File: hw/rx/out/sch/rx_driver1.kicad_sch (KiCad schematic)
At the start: 24 parts, among them U6 OPA1656

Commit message: hw/rx: review fixes for #81 (mute relay + supervisor, S1J clamps, VCM discharge + 2-pole filter, 16 V LDOs, keyed header, I2S DNP, cable stability + power-cycle SPICE, FLT low latency) (#32)
Co-Authored-By: Claude Opus 5.5 <noreply@anthropic.com>
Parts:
- added C49: 22u 25V, Capacitor_SMD:CP_Elec_5x5.4, symbol openpack_rx:CP
- added D5, D6: S1J, Diode_SMD:D_SMA, symbol openpack_rx:Diode
- added D8: BAT54, Package_TO_SOT_SMD:SOT-23, symbol openpack_rx:BAT54
- added K1: TQ2SA-12V, openpack:Panasonic_TQ2SA, symbol openpack_rx:Relay_TQ2
- added R53, R54, R55: 10k, Resistor_SMD:R_0402_1005Metric, symbol openpack_rx:R
- C43: value 47u 25V -> 22u 25V; MPN ALU_47u_25V -> ALU_22u_25V
- D3, D4: value BAV99 -> S1J; footprint Package_TO_SOT_SMD:SOT-23 -> Diode_SMD:D_SMA; symbol openpack_rx:BAV99 -> openpack_rx:Diode; MPN BAV99,215 -> S1J
- R45, R46: value 100k -> 22k
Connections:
- net +12VA: now also C41.2, C44.1, R42.2, R43.1, R47.1, U6.1 (OUTA), U6.3 (+INA), U6.5 (+INB), C49.1 (+), D5.1 (K), D6.1 (K), D8.1 (A), D8.3 (K), R53.2; no longer D3.2 (K2), D4.2 (K2)
- net GND: now also C43.1 (+), D3.2 (A), D4.2 (A), R45.2, R46.1, C49.2 (-), R53.1, R54.2, R55.2; no longer C40.2 (-), C42.1, C42.2, C47.1, C48.1, D3.1 (A1), D3.3 (COM), D4.1 (A1), D4.3 (COM), R43.2, R44.1, R44.2, R47.2, R50.1, R50.2, U6.6 (-INB), U6.7 (OUTB)
- net DRV_CIN: now reaches C40.1 (+), R41.1
- net DRV_HOT_O: now reaches R51.1, R52.1
- net DRV_HOT_O: now also K1.7 (NO2); no longer C48.2
- net DRV_COLD_O: now reaches R48.1, R49.1
- net DRV_COLD_O: now also K1.4 (NO1); no longer C47.2
- removed net DRV_OUTA: C41.2, C43.1 (+), C44.1, R42.2, R43.1, R45.2, R46.1, R47.1, U6.1 (OUTA), U6.3 (+INA), U6.5 (+INB)
- new net +12V: K1.1 (COIL+)
- new net DAC_OUTF: C40.2 (-)
- new net DRV_COLD_P: C47.1, D3.1 (K), D5.2 (A), R47.2
- new net DRV_COLD_X: C47.2, K1.3 (COM1), R54.1
- new net DRV_HOT_P: C42.1, C42.2, C48.1, D4.1 (K), D6.2 (A), R43.2, R44.1, R44.2, R50.1, R50.2, U6.6 (-INB), U6.7 (OUTB)
- new net DRV_HOT_X: C48.2, K1.8 (COM2), R55.1
- new net RLY_COIL: K1.10 (COIL-)
- no-connect marks 0 -> 5
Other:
- moved on the sheet: C40, C41, C42, C43, C44, C45, C46, C47, C48, R41, R42, R43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

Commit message: hw/rx: receiver module BT40NE -> BT40E, FEM node pack-only (ADR-0021, #112)
- hw/rx: BT40E symbol (Fanstel v1.09 p.14 pad map = BT40F/NE names), footprint
  openpack:Fanstel_BT40E (14x16 mm), no FEM nets, P1.05 open; GPIO map unchanged.
  ERC 0/0. BOM: Digi-Key UK GBP 9.7765 q100 -> $30.68 / GBP 23.38 per sub-board.
- fw: receiver builds add boards/role_rx_cpunet.overlay (FEM node disabled, no
  &radio fem); rx.c refuses to build with the FEM enabled.
- ADR-0014 amended (datasheet checks, FCC X8WBT40F, no UKCA DoC, BOM).

Co-Authored-By: Claude Opus 5.5 <noreply@anthropic.com>
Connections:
- net DRV_HOT_P is gone; now on net DAC_OUTF: C42.1, C42.2, C48.1, D4.1 (K), D6.2 (A), R43.2, R44.1, R44.2, R50.1, R50.2, U6.6 (-INB), U6.7 (OUTB)
- net +12VA: no longer C41.2, C44.1, C49.1 (+), D8.1 (A), R42.2, R43.1, R47.1, R53.2, U6.1 (OUTA), U6.3 (+INA), U6.5 (+INB)
- net DRV_CIN: no longer names the net of C40.1 (+), R41.1
- new net DRV_OUTA: C41.2, C44.1, C49.1 (+), D8.1 (A), R42.2, R43.1, R47.1, R53.2, U6.1 (OUTA), U6.3 (+INA), U6.5 (+INB)
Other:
- moved on the sheet: C40, C41, C42, C43, C44, C45, C46, C47, C48, C49, D3, D4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

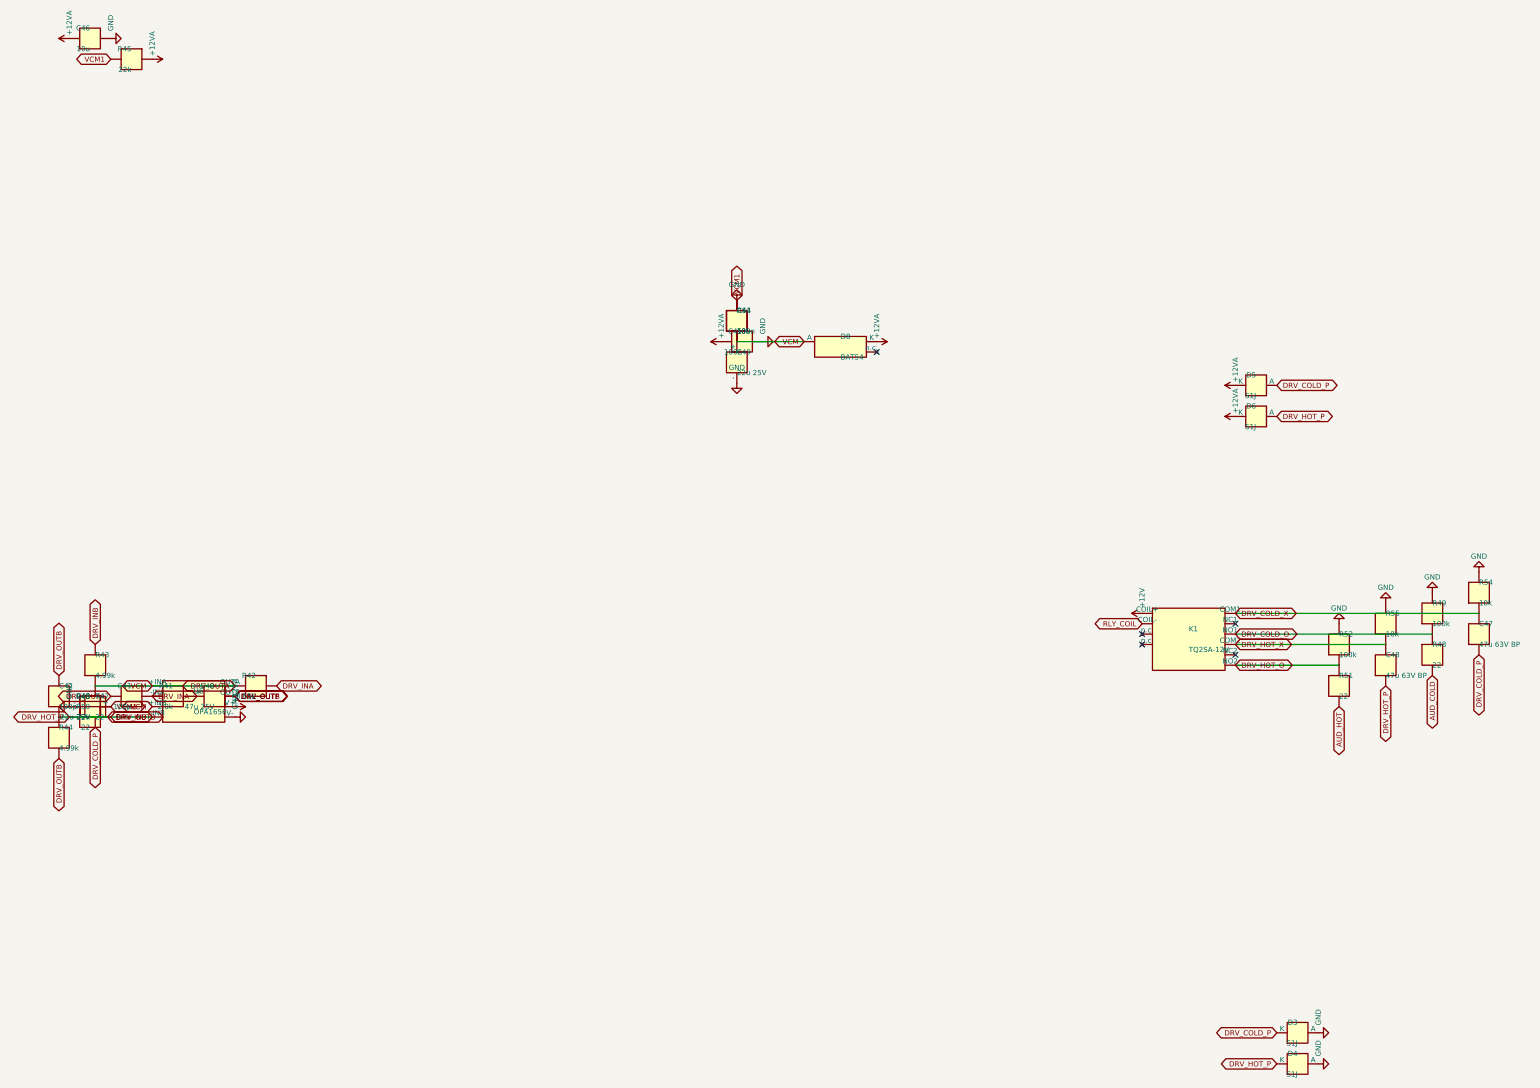
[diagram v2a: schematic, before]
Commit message: hw/rx: receiver sub-board layout, 50 ohm GCPW, keyed J1, JLC rules that load, fab outputs (#34) (#116)
Part of #34. Receiver layout (48x90 mm, DRC 0/0), #116 independent-review fixes (netclass pour clearances in rx + pack, no hole at J1 pin 14, solid RF grounds, K1 pin-1/CPL), every placed part with a checked LCSC code.

Co-Authored-By: Claude Opus 5.5 <noreply@anthropic.com>
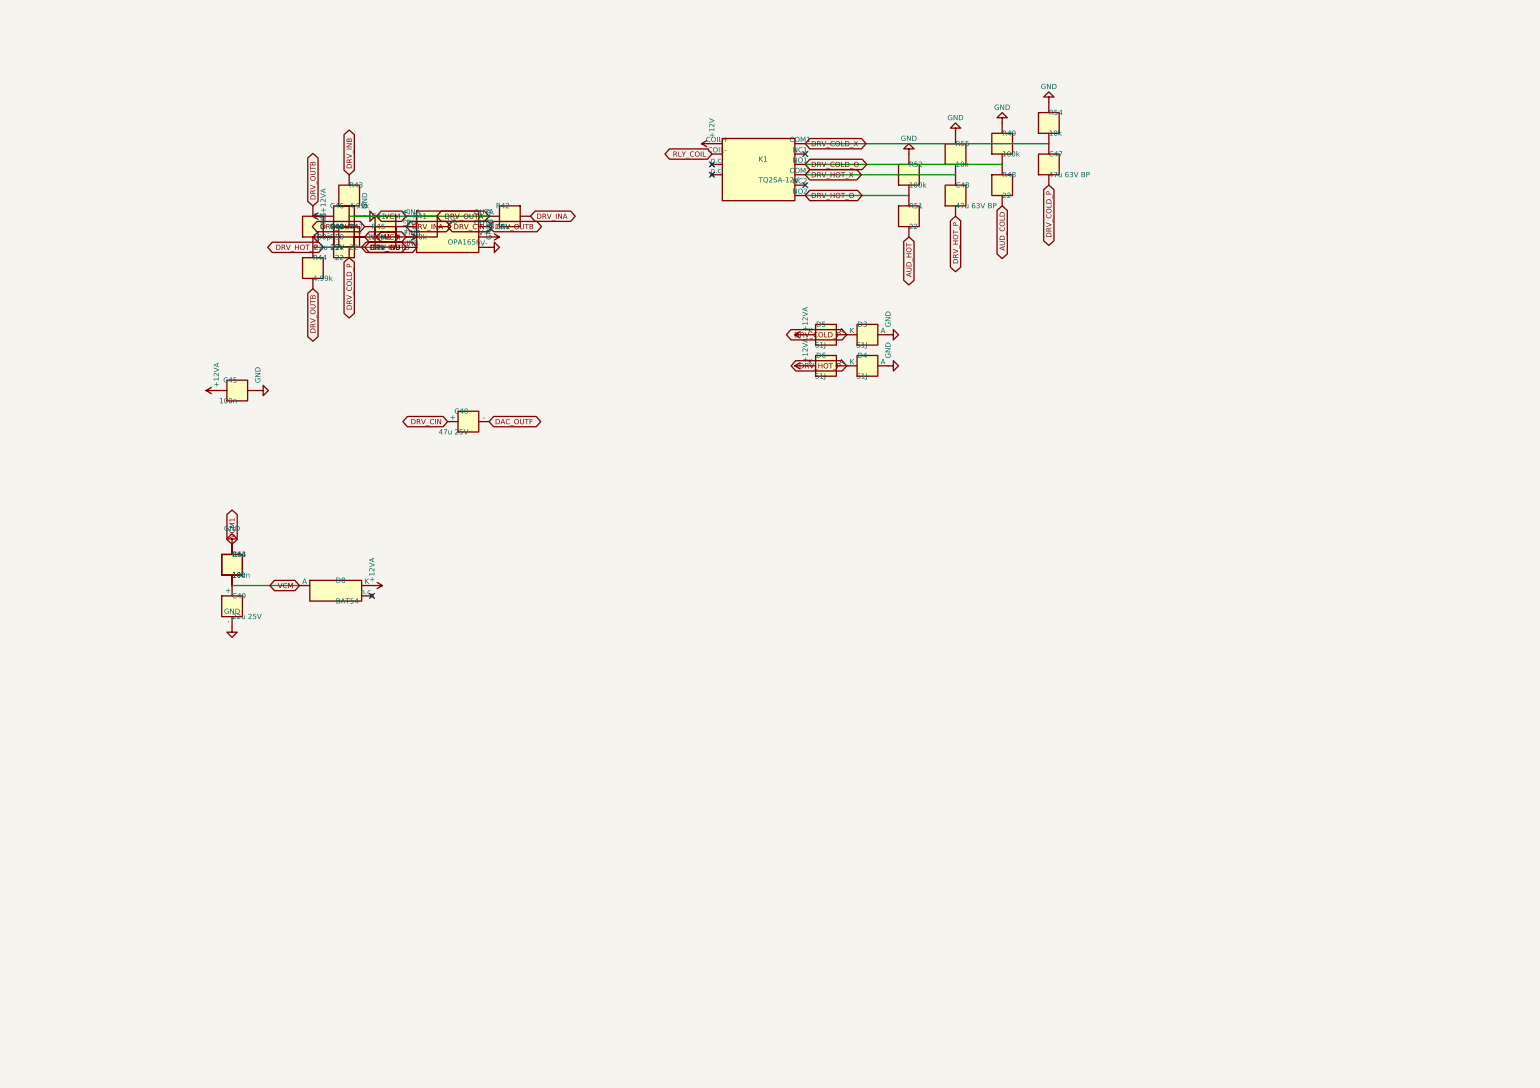
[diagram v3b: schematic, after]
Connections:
- net DRV_OUTA is gone; now on net +12VA: C41.2, C44.1, C49.1 (+), D8.1 (A), R42.2, R43.1, R47.1, R53.2, U6.1 (OUTA), U6.3 (+INA), U6.5 (+INB)
- net DAC_OUTF: no longer C42.1, C42.2, C48.1, D4.1 (K), D6.2 (A), R43.2, R44.1, R44.2, R50.1, R50.2, U6.6 (-INB), U6.7 (OUTB)
- net DRV_CIN: now reaches C40.1 (+), R41.1
- new net DRV_HOT_P: C42.1, C42.2, C48.1, D4.1 (K), D6.2 (A), R43.2, R44.1, R44.2, R50.1, R50.2, U6.6 (-INB), U6.7 (OUTB)
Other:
- moved on the sheet: C40, C41, C42, C43, C44, C45, C46, C47, C48, C49, D3, D4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
